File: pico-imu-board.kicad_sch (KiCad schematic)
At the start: 9 parts, among them J1 USB_B_Micro, U1 RP2040, U2 MPU-9250, U3 NCP1117-3.3_SOT223

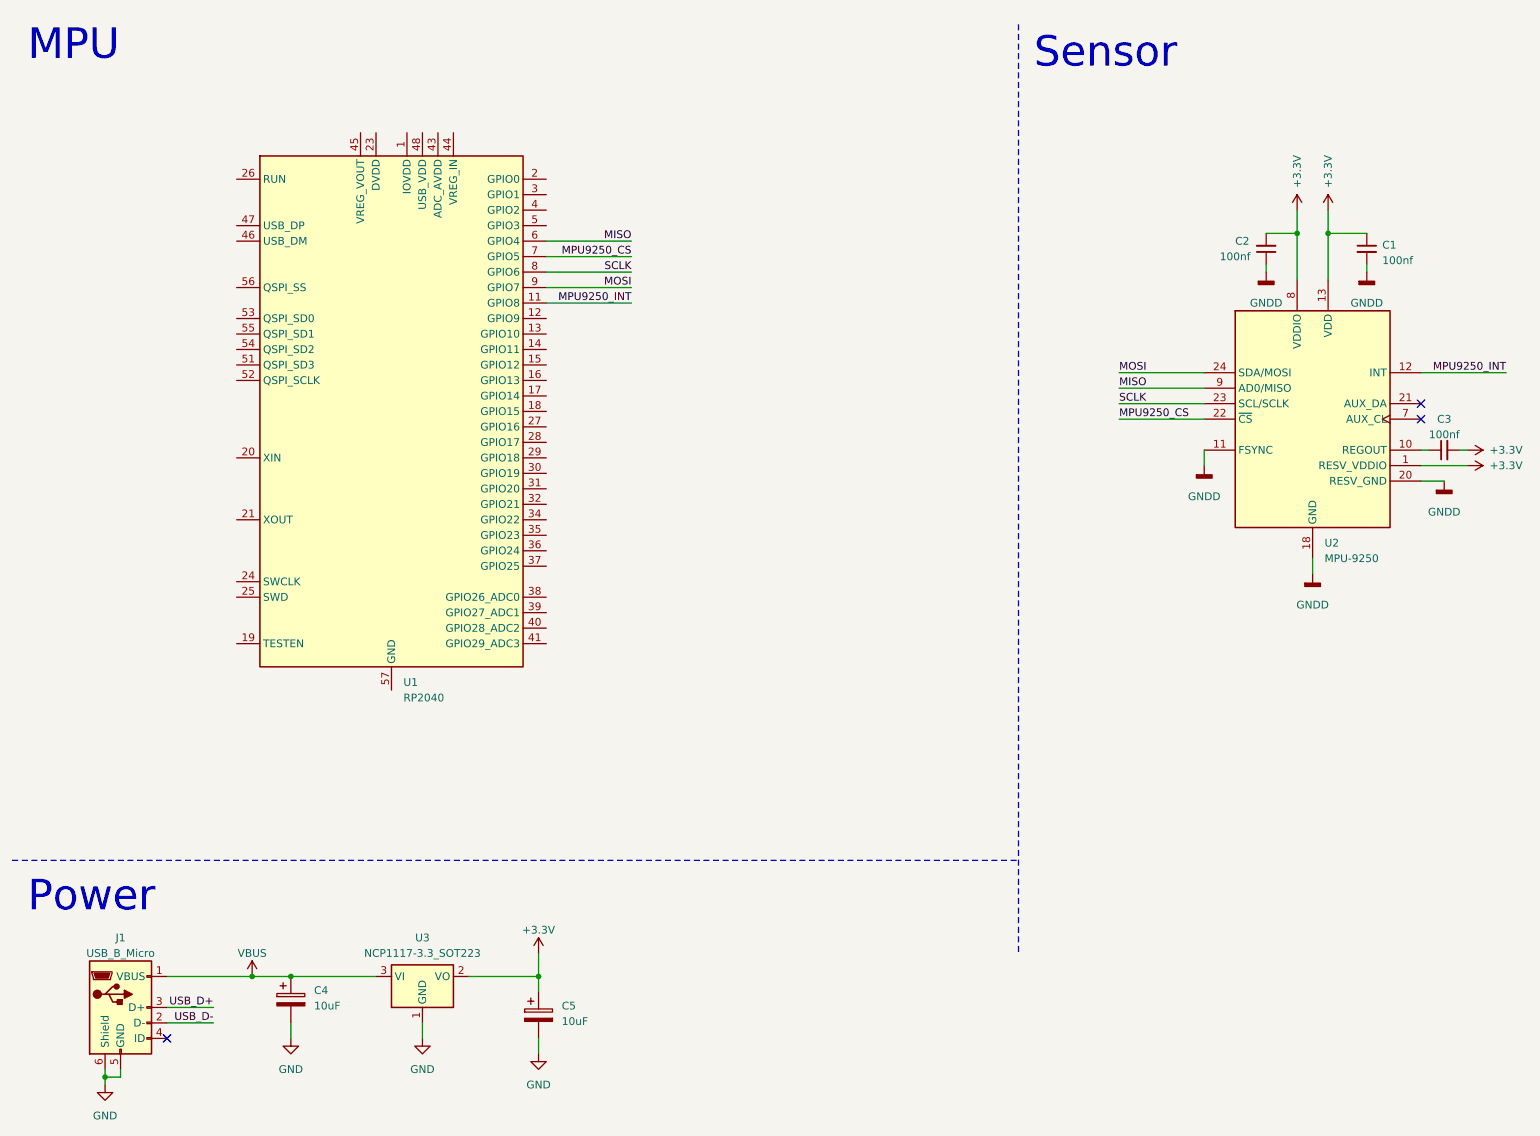
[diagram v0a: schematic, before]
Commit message: Added decoupling capacitors
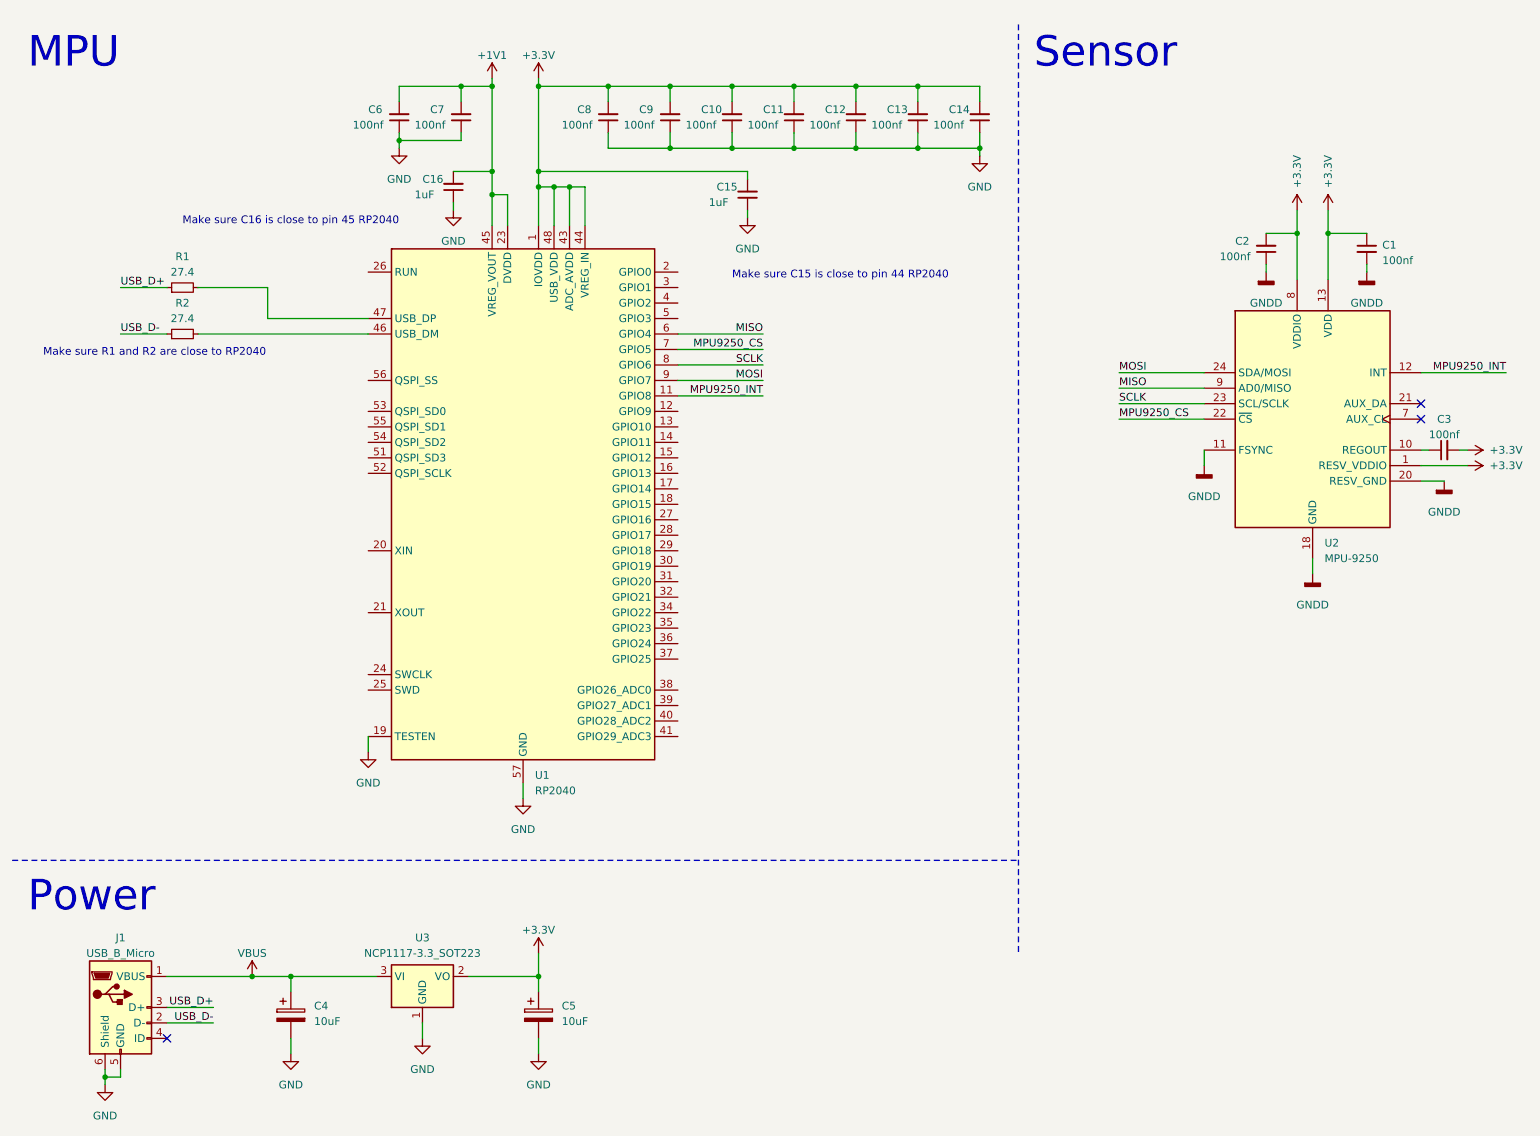
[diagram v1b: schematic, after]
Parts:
- added C10, C11, C12, C13, C14, C6, C7, C8, C9: 100nf, Capacitor_SMD:C_0402_1005Metric, symbol Device:C_Small
- added C15, C16: 1uF, Capacitor_SMD:C_0805_1005Metric, symbol Device:C_Small
- added R1, R2: 27.4, Resistor_SMD:R_0402_1005Metric, symbol Device:R_Small
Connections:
- net +3.3V: now also U1.1 (IOVDD), U1.10 (IOVDD), U1.22 (IOVDD), U1.33 (IOVDD), U1.42 (IOVDD), U1.43 (ADC_AVDD), U1.44 (VREG_IN), U1.48 (USB_VDD), U1.49 (IOVDD), C10.2, C11.2, C12.2, C13.2, C14.2, C15.2, C8.2, C9.2
- net GND: now also U1.19 (TESTEN), U1.57 (GND), C10.1, C11.1, C12.1, C13.1, C14.1, C15.1, C16.1, C6.1, C7.1, C8.1, C9.1
- net USB_D+: now also R1.1
- net USB_D-: now also R2.1
- net +1V1: now reaches U1.23 (DVDD), U1.50 (DVDD)
- net +1V1: now also U1.45 (VREG_VOUT), C16.2, C6.2, C7.2
- net at U1.46 (USB_DM): now also R2.2
- net at U1.47 (USB_DP): now also R1.2
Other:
- note added: "Make sure C15 is close to pin 44 RP2040"
- note added: "Make sure C16 is close to pin 45 RP2040"
- note added: "Make sure R1 and R2 are close to RP2040"
- moved on the sheet: C4, U1
